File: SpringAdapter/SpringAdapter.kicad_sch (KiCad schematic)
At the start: 17 parts, among them J1 USB_C_Receptacle_USB2.0, J2 Conn_02x04_Odd_Even, SW1 SW_DIP_x01, U1 AP2112K-3.3

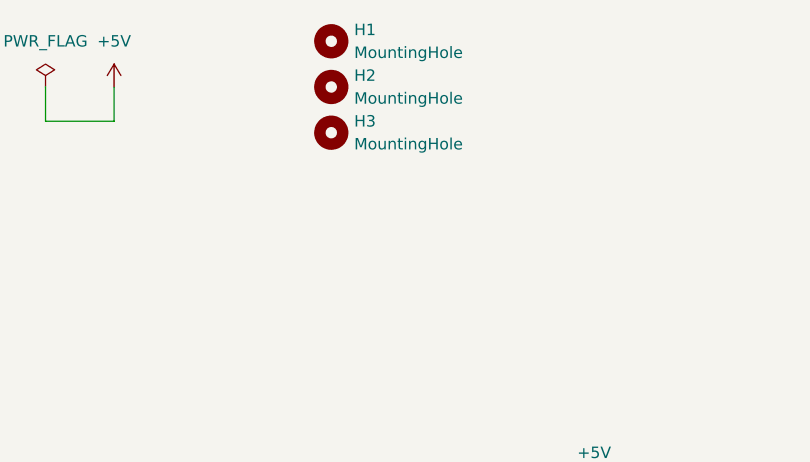
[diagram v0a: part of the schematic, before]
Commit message: Add second mounting hole
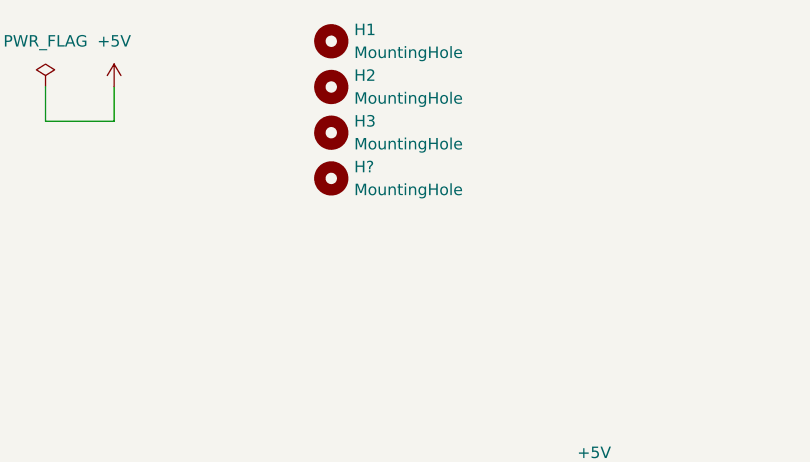
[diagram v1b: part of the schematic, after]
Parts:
- added H?: MountingHole, MountingHole:MountingHole_2.5mm, symbol Mechanical:MountingHole
- H3: footprint MountingHole:MountingHole_2.1mm -> MountingHole:MountingHole_2.5mm
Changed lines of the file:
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@@
       (effects (font (size 1.27 1.27)) (justify left))
     )
-    (property "Footprint" "MountingHole:MountingHole_2.1mm" (id 2) (at 77.47 29.21 0)
+    (property "Footprint" "MountingHole:MountingHole_2.5mm" (id 2) (at 77.47 29.21 0)
       (effects (font (size 1.27 1.27)) hide)
     )
@@
     (pin "2")
   )
+  (symbol (lib_id "Mechanical:MountingHole") (at 77.47 34.29 0) (unit 1)
+    (in_bom yes) (on_board yes) (fields_autoplaced)
+    (property "Reference" "H?" (id 0) (at 80.01 33.0199 0)
+      (effects (font (size 1.27 1.27)) (justify left))
+    )
+    (property "Value" "MountingHole" (id 1) (at 80.01 35.5599 0)
+      (effects (font (size 1.27 1.27)) (justify left))
+    )
+    (property "Footprint" "MountingHole:MountingHole_2.5mm" (id 2) (at 77.47 34.29 0)
+      (effects (font (size 1.27 1.27)) hide)
+    )
+    (property "Datasheet" "~" (id 3) (at 77.47 34.29 0)
+      (effects (font (size 1.27 1.27)) hide)
+    )
+  )
   (sheet_instances
     (path "/" (page "1"))
@@
     )
     (path "/d3ab0cd1-9b88-4919-a40c-c6fccd3539ec"
-      (reference "H3") (unit 1) (value "MountingHole") (footprint "MountingHole:MountingHole_2.1mm")
+      (reference "H3") (unit 1) (value "MountingHole") (footprint "MountingHole:MountingHole_2.5mm")
+    )
+    (path "/f97e48c1-64cd-443b-afc2-48fe73a19f0d"
+      (reference "H?") (unit 1) (value "MountingHole") (footprint "MountingHole:MountingHole_2.5mm")
     )
     (path "/ee15ac4f-84b7-427d-93b4-b771dd2d0c48"

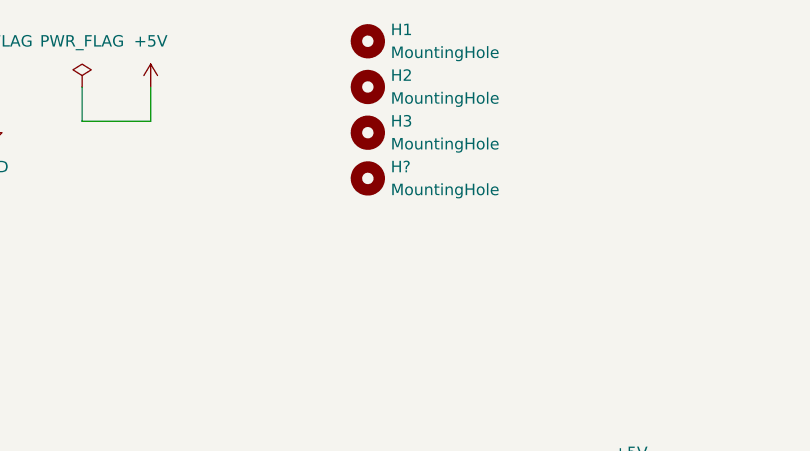
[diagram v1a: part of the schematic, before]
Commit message: Spring adapter add drawing and second mounting hole
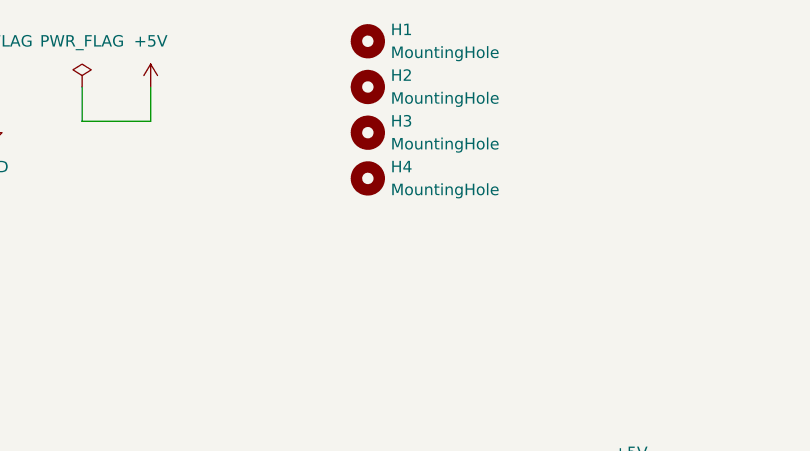
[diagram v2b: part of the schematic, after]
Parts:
- gave numbers to parts that had none: 1
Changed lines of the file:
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@@
   (symbol (lib_id "Mechanical:MountingHole") (at 77.47 34.29 0) (unit 1)
     (in_bom yes) (on_board yes) (fields_autoplaced)
-    (property "Reference" "H?" (id 0) (at 80.01 33.0199 0)
+    (property "Reference" "H4" (id 0) (at 80.01 33.0199 0)
       (effects (font (size 1.27 1.27)) (justify left))
     )
@@
     )
     (path "/f97e48c1-64cd-443b-afc2-48fe73a19f0d"
-      (reference "H?") (unit 1) (value "MountingHole") (footprint "MountingHole:MountingHole_2.5mm")
+      (reference "H4") (unit 1) (value "MountingHole") (footprint "MountingHole:MountingHole_2.5mm")
     )
     (path "/ee15ac4f-84b7-427d-93b4-b771dd2d0c48"

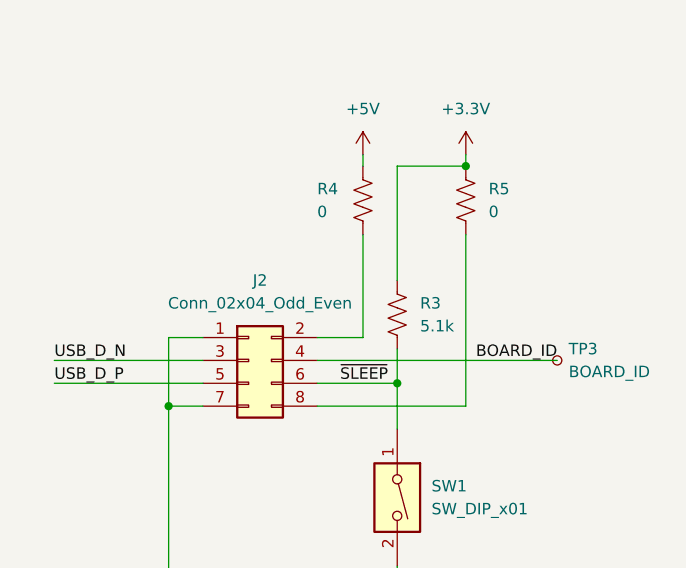
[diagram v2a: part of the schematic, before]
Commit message: correct spring position
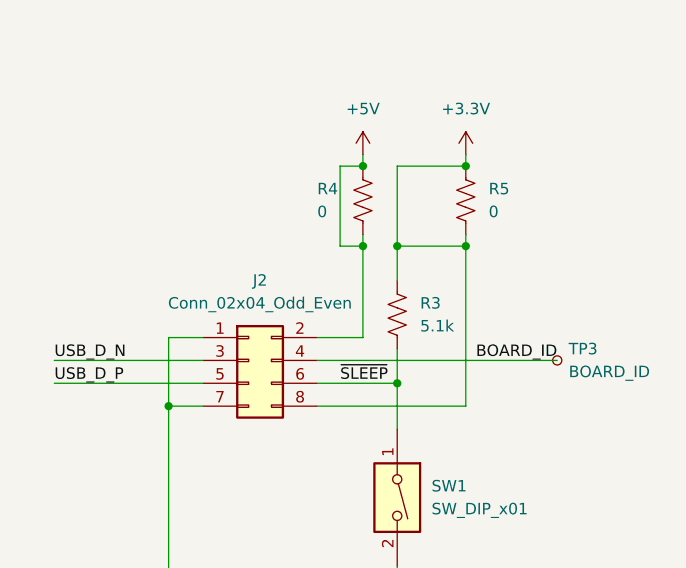
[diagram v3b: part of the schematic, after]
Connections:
- net +3.3V: now also J2.8 (Pin_8), R5.2
- net +5V: now also J2.2 (Pin_2), R4.2
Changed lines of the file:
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@@
 (kicad_sch (version 20211123) (generator eeschema)
   (paper "A4")
+  (junction (at 226.06 77.47) (diameter 0) (color 0 0 0 0)
+  )
   (junction (at 226.06 68.58) (diameter 0) (color 0 0 0 0)
   )
   (junction (at 147.32 91.44) (diameter 0) (color 0 0 0 0)
   )
+  (junction (at 214.63 77.47) (diameter 0) (color 0 0 0 0)
+  )
   (junction (at 158.75 74.93) (diameter 0) (color 0 0 0 0)
   )
@@
   (junction (at 106.68 127) (diameter 0) (color 0 0 0 0)
   )
+  (junction (at 218.44 77.47) (diameter 0) (color 0 0 0 0)
+  )
   (junction (at 135.89 77.47) (diameter 0) (color 0 0 0 0)
   )
   (junction (at 68.58 127) (diameter 0) (color 0 0 0 0)
+  )
+  (junction (at 214.63 68.58) (diameter 0) (color 0 0 0 0)
   )
   (no_connect (at 83.82 107.95))
@@
     (stroke (width 0) (type default) (color 0 0 0 0))
   )
+  (wire (pts (xy 214.63 77.47) (xy 212.09 77.47))
+    (stroke (width 0) (type default) (color 0 0 0 0))
+  )
   (wire (pts (xy 218.44 92.71) (xy 218.44 97.79))
     (stroke (width 0) (type default) (color 0 0 0 0))
   )
+  (wire (pts (xy 226.06 77.47) (xy 226.06 95.25))
+    (stroke (width 0) (type default) (color 0 0 0 0))
+  )
   (wire (pts (xy 68.58 118.11) (xy 68.58 127))
     (stroke (width 0) (type default) (color 0 0 0 0))
@@
     (stroke (width 0) (type default) (color 0 0 0 0))
   )
-  (wire (pts (xy 218.44 68.58) (xy 218.44 81.28))
+  (wire (pts (xy 218.44 68.58) (xy 218.44 77.47))
     (stroke (width 0) (type default) (color 0 0 0 0))
   )
@@
     (stroke (width 0) (type default) (color 0 0 0 0))
   )
+  (wire (pts (xy 218.44 77.47) (xy 218.44 81.28))
+    (stroke (width 0) (type default) (color 0 0 0 0))
+  )
   (wire (pts (xy 209.55 87.63) (xy 214.63 87.63))
     (stroke (width 0) (type default) (color 0 0 0 0))
@@
     (stroke (width 0) (type default) (color 0 0 0 0))
   )
-  (wire (pts (xy 214.63 76.2) (xy 214.63 87.63))
+  (wire (pts (xy 214.63 76.2) (xy 214.63 77.47))
     (stroke (width 0) (type default) (color 0 0 0 0))
   )
@@
     (stroke (width 0) (type default) (color 0 0 0 0))
   )
+  (wire (pts (xy 218.44 77.47) (xy 226.06 77.47))
+    (stroke (width 0) (type default) (color 0 0 0 0))
+  )
   (wire (pts (xy 87.63 92.71) (xy 87.63 95.25))
     (stroke (width 0) (type default) (color 0 0 0 0))
@@
     (stroke (width 0) (type default) (color 0 0 0 0))
   )
+  (wire (pts (xy 212.09 77.47) (xy 212.09 68.58))
+    (stroke (width 0) (type default) (color 0 0 0 0))
+  )
   (wire (pts (xy 196.85 87.63) (xy 193.04 87.63))
     (stroke (width 0) (type default) (color 0 0 0 0))
@@
     (stroke (width 0) (type default) (color 0 0 0 0))
   )
+  (wire (pts (xy 214.63 77.47) (xy 214.63 87.63))
+    (stroke (width 0) (type default) (color 0 0 0 0))
+  )
   (wire (pts (xy 196.85 95.25) (xy 193.04 95.25))
     (stroke (width 0) (type default) (color 0 0 0 0))
@@
     (stroke (width 0) (type default) (color 0 0 0 0))
   )
-  (wire (pts (xy 226.06 76.2) (xy 226.06 95.25))
-    (stroke (width 0) (type default) (color 0 0 0 0))
-  )
+  (wire (pts (xy 226.06 76.2) (xy 226.06 77.47))
+    (stroke (width 0) (type default) (color 0 0 0 0))
+  )
+  (wire (pts (xy 212.09 68.58) (xy 214.63 68.58))
+    (stroke (width 0) (type default) (color 0 0 0 0))
+  )

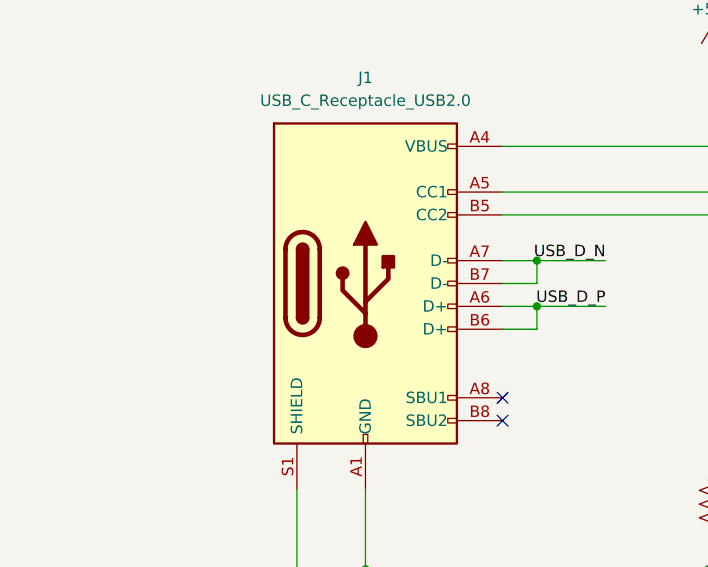
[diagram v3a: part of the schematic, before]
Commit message: Switch to pogo pins
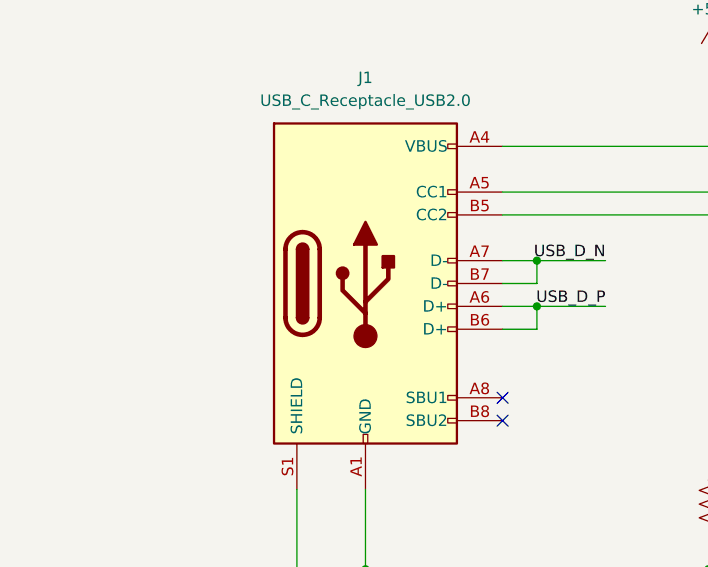
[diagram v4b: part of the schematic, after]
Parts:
- J2: footprint SpringAdapter:ABTBA018_2x4_P1.6mm -> SpringAdapter:BP33242_2x4_P2.0mm
